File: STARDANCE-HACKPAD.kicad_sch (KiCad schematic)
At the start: 2 parts, among them J1 Conn_01x04_Socket, U1 MOUDLE-SEEEDUINO-XIAO

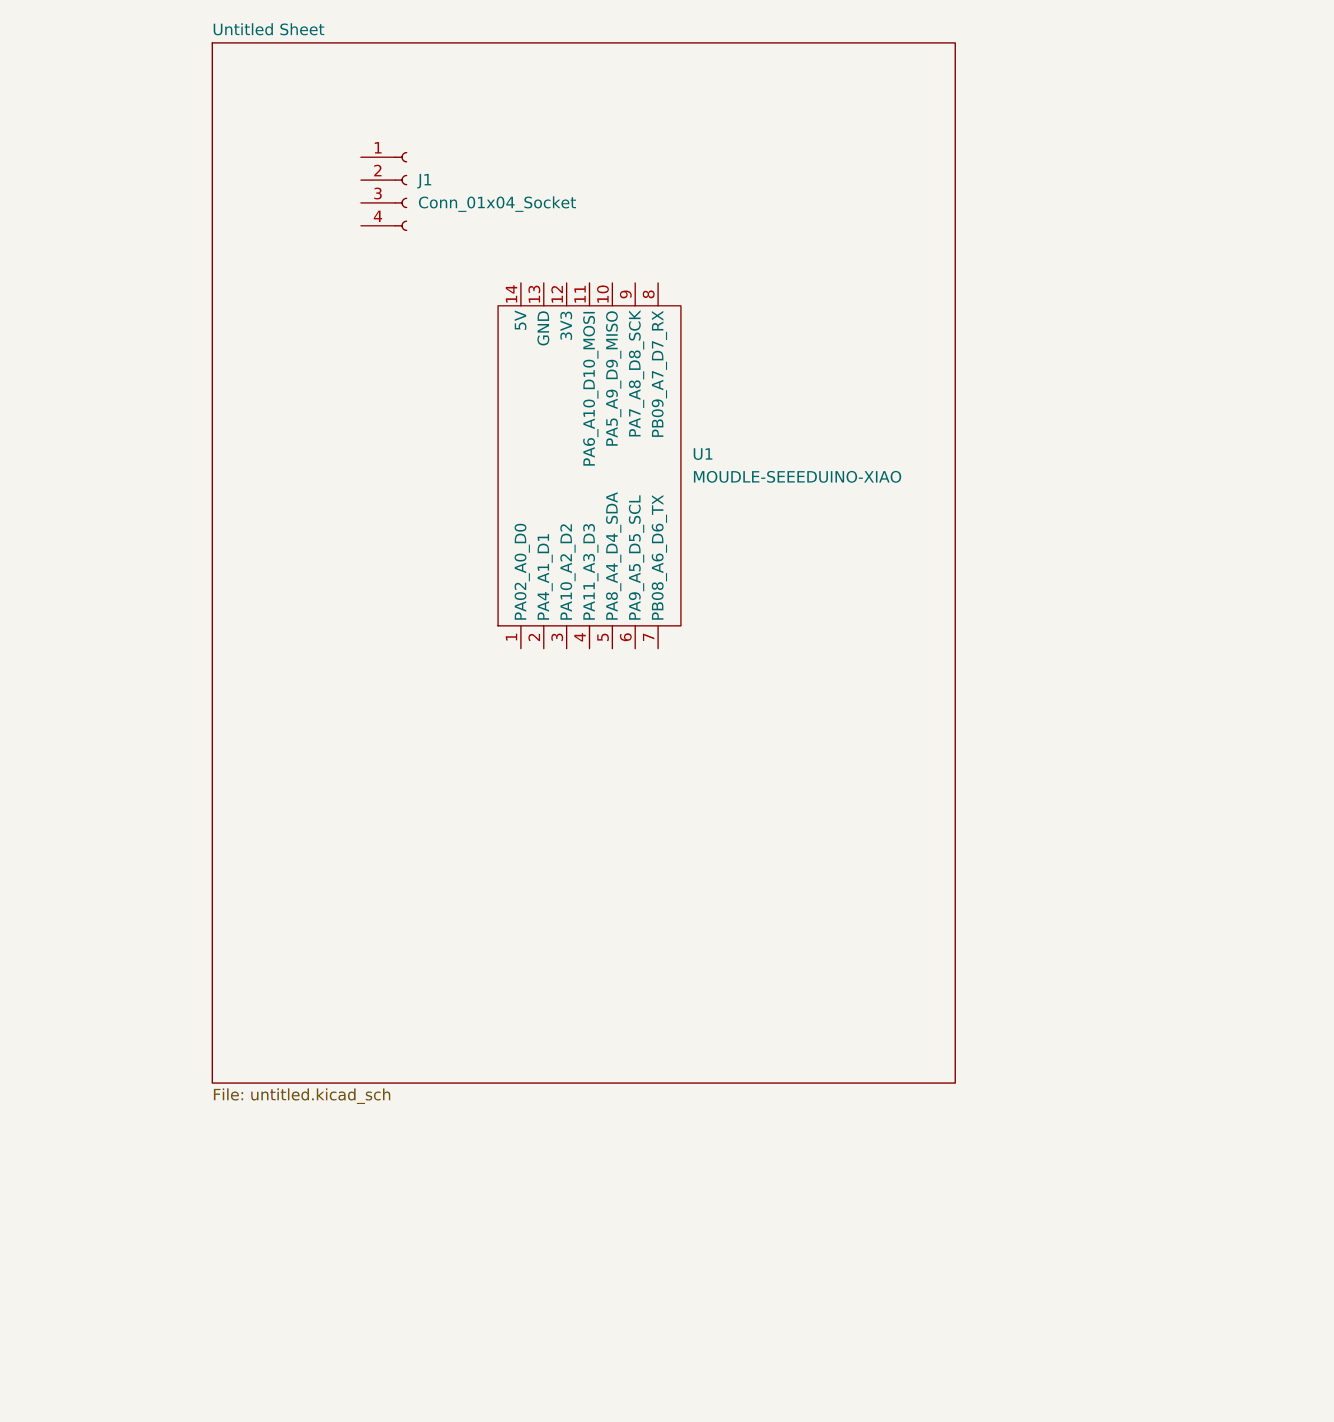
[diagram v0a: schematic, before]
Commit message: updated kicad finished schematic
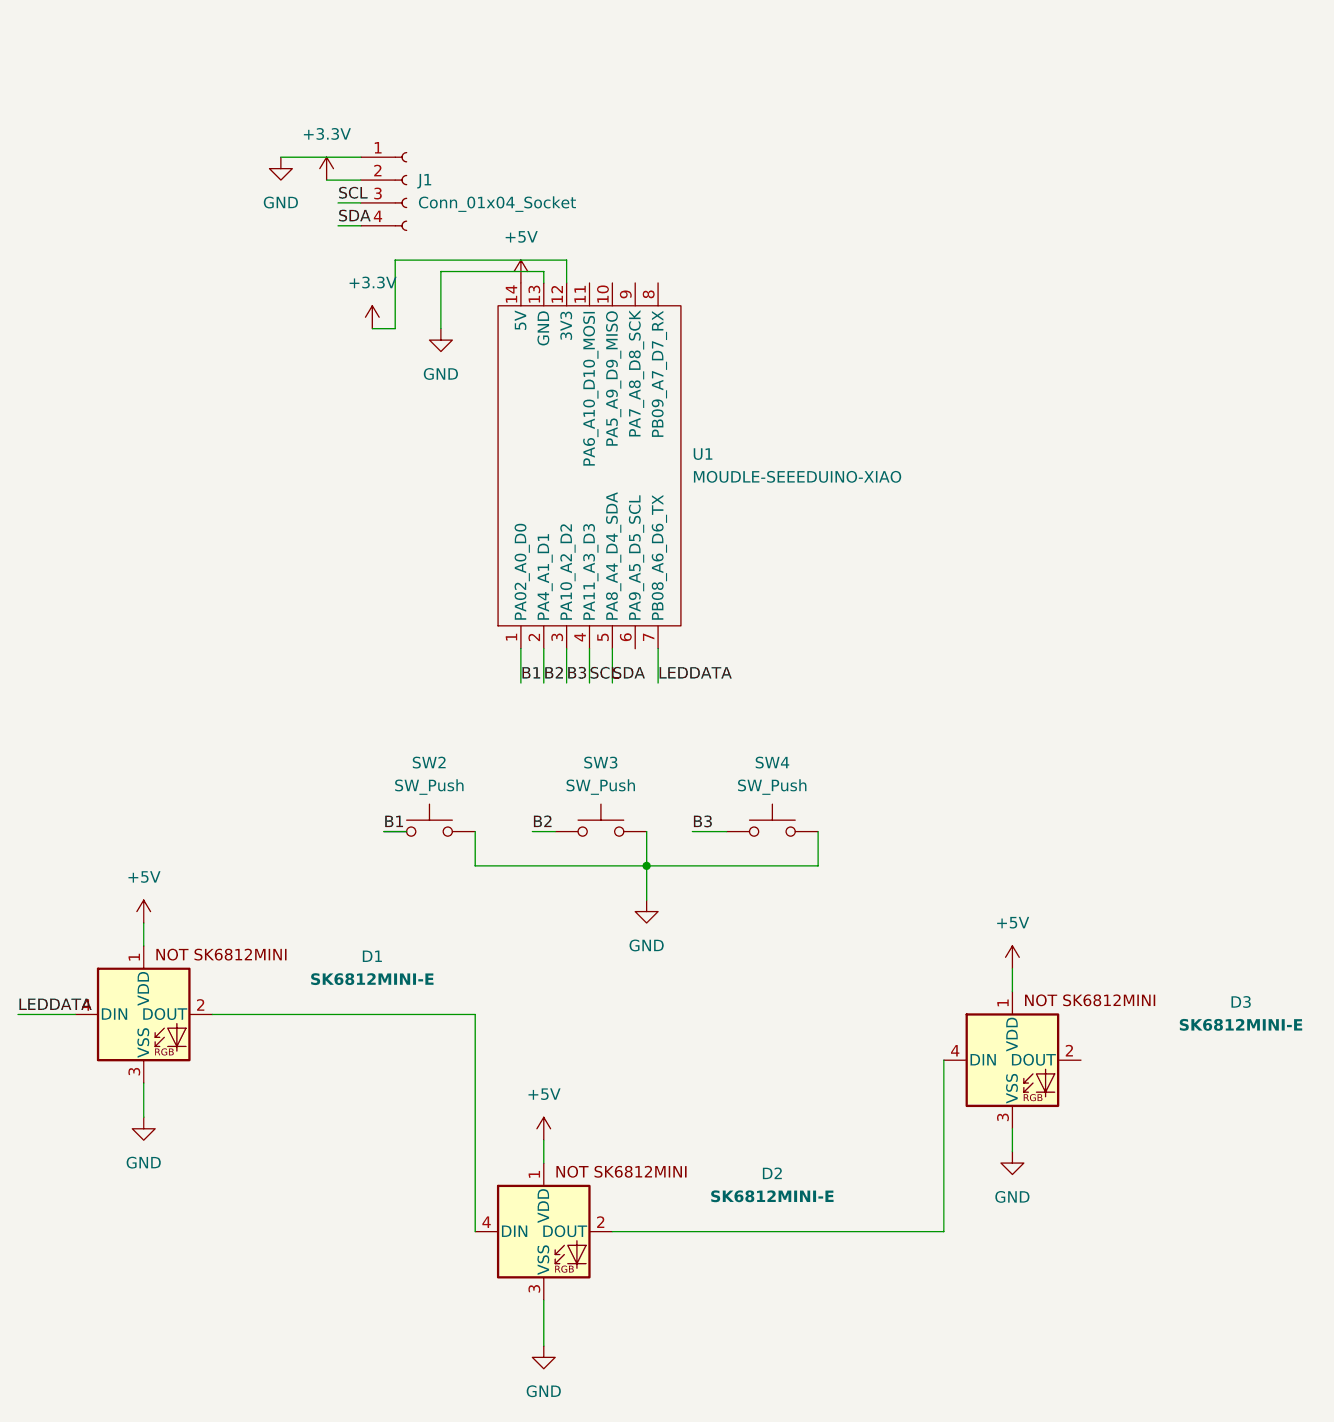
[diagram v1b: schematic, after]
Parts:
- added D1, D2, D3: SK6812MINI-E, SK6812MINI-E - 3.2x2.8x1.78mm, symbol SK6812MINI-E:SK6812MINI-E
- added SW2, SW3, SW4: SW_Push, symbol Switch:SW_Push
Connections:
- net GND: now reaches J1.1 (Pin_1)
- net GND: now also U1.13 (GND), D1.3 (VSS), D2.3 (VSS), D3.3 (VSS), SW2.2, SW3.2, SW4.2
- net +3.3V: now reaches J1.2 (Pin_2)
- net +3.3V: now also U1.12 (3V3)
- net SCL: now reaches J1.3 (Pin_3)
- net SCL: now also U1.4 (PA11_A3_D3)
- net SDA: now reaches J1.4 (Pin_4)
- net SDA: now also U1.5 (PA8_A4_D4_SDA)
- net B1: now reaches U1.1 (PA02_A0_D0)
- net B1: now also SW2.1
- net +5V: now reaches U1.14 (5V)
- net +5V: now also D1.1 (VDD), D2.1 (VDD), D3.1 (VDD)
- net B2: now reaches U1.2 (PA4_A1_D1)
- net B2: now also SW3.1
- net B3: now reaches U1.3 (PA10_A2_D2)
- net B3: now also SW4.1
- net LEDDATA: now reaches U1.7 (PB08_A6_D6_TX)
- net LEDDATA: now also D1.4 (DIN)
- new net: D1.2 (DOUT), D2.4 (DIN)
- new net: D2.2 (DOUT), D3.4 (DIN)
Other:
- removed sheet Untitled Sheet

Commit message: Worked on PCB, starting to journal the day's work.
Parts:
- D1, D2, D3: footprint SK6812MINI-E - 3.2x2.8x1.78mm -> LED_SMD:LED_SK6812MINI-E_3.2x2.8mm_P1.5mm_ReverseMount
- J1: footprint (none) -> Connector_PinHeader_2.54mm:PinHeader_1x04_P2.54mm_Vertical
- SW2, SW3, SW4: footprint (none) -> Button_Switch_Keyboard:SW_Cherry_MX_1.00u_Plate
- U1: footprint (none) -> Connector_PinHeader_2.54mm:PinHeader_2x07_P2.54mm_Vertical
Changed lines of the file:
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@@
 			)
 		)
-		(property "Footprint" ""
+		(property "Footprint" "Button_Switch_Keyboard:SW_Cherry_MX_1.00u_Plate"
 			(at 184.15 109.22 0)
 			(hide yes)
@@
 			)
 		)
-		(property "Footprint" "SK6812MINI-E - 3.2x2.8x1.78mm"
+		(property "Footprint" "LED_SMD:LED_SK6812MINI-E_3.2x2.8mm_P1.5mm_ReverseMount"
 			(at 115.57 142.24 0)
 			(hide yes)
@@
 			)
 		)
-		(property "Footprint" "SK6812MINI-E - 3.2x2.8x1.78mm"
+		(property "Footprint" "LED_SMD:LED_SK6812MINI-E_3.2x2.8mm_P1.5mm_ReverseMount"
 			(at 160.02 166.37 0)
 			(hide yes)
@@
 			)
 		)
-		(property "Footprint" "SK6812MINI-E - 3.2x2.8x1.78mm"
+		(property "Footprint" "LED_SMD:LED_SK6812MINI-E_3.2x2.8mm_P1.5mm_ReverseMount"
 			(at 212.09 147.32 0)
 			(hide yes)
@@
 			)
 		)
-		(property "Footprint" ""
+		(property "Footprint" "Button_Switch_Keyboard:SW_Cherry_MX_1.00u_Plate"
 			(at 146.05 109.22 0)
 			(hide yes)
@@
 			)
 		)
-		(property "Footprint" ""
+		(property "Footprint" "Connector_PinHeader_2.54mm:PinHeader_1x04_P2.54mm_Vertical"
 			(at 143.51 41.91 0)
 			(hide yes)
@@
 			)
 		)
-		(property "Footprint" ""
+		(property "Footprint" "Connector_PinHeader_2.54mm:PinHeader_2x07_P2.54mm_Vertical"
 			(at 161.29 91.44 0)
 			(hide yes)
@@
 			)
 		)
-		(property "Footprint" ""
+		(property "Footprint" "Button_Switch_Keyboard:SW_Cherry_MX_1.00u_Plate"
 			(at 165.1 109.22 0)
 			(hide yes)
